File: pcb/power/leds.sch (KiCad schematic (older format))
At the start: 20 parts, among them P6 CONN_01X04, U3 LM324QT

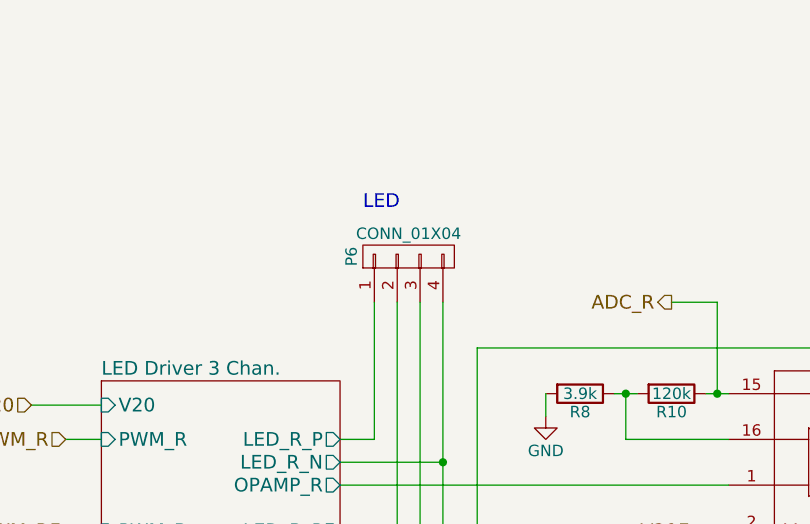
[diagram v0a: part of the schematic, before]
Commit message: Started layouting. Interfacing problems have to be discussed.
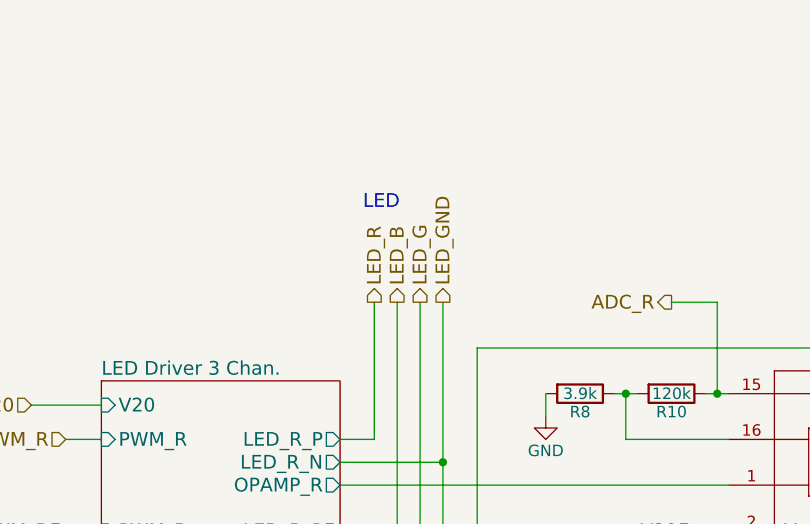
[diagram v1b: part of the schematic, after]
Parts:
- removed P6: CONN_01X04, Connect:PINHEAD1-3, symbol CONN_01X04
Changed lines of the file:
@@
-$EndComp
-$Comp
-L CONN_01X04 P6
-U 1 1 58430FB4
-P 4000 2500
-F 0 "P6" H 4000 2750 50  0000 C CNN
-F 1 "CONN_01X04" V 4100 2500 50  0000 C CNN
-F 2 "Connect:PINHEAD1-3" H 4000 2500 50  0001 C CNN
-F 3 "http://www.on-shore.com/wp-content/uploads/2015/09/ostvnxxa150.pdf" H 4000 2500 50  0001 C CNN
-F 4 "ED10563-ND" H 4000 2500 60  0001 C CNN "Digikey"
-	1    4000 2500
-	0    -1   -1   0
 $EndComp
 $Comp
@@
 Text HLabel 7450 2150 2    60   Output ~ 0
 VOLED
+Text HLabel 3850 2700 1    60   Output ~ 0
+LED_R
+Text HLabel 3950 2700 1    60   Output ~ 0
+LED_B
+Text HLabel 4050 2700 1    60   Output ~ 0
+LED_G
+Text HLabel 4150 2700 1    60   Output ~ 0
+LED_GND
 $EndSCHEMATC

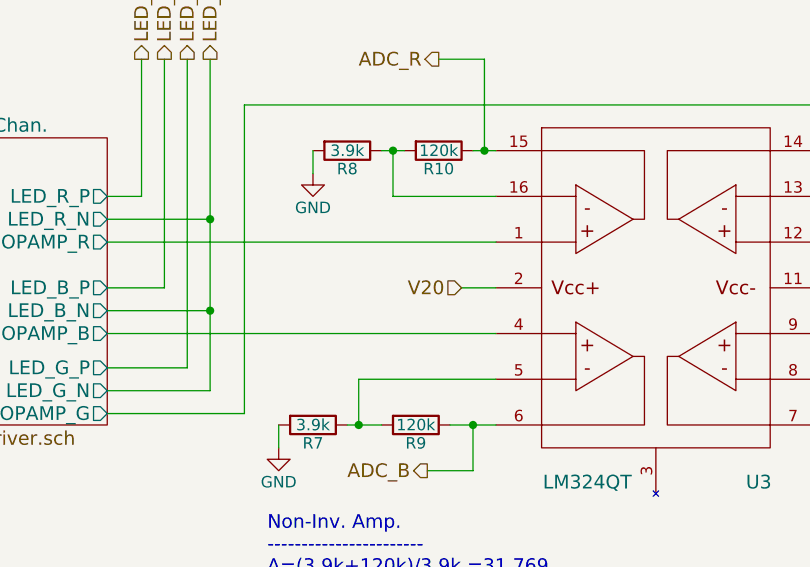
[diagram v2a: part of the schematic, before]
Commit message: Did a lot of stuff. Currently working on the exact 3D models for the headers.
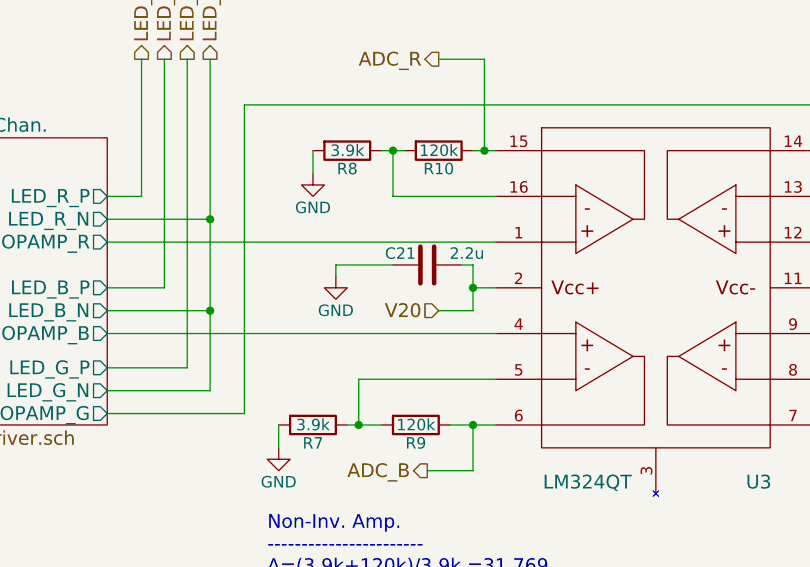
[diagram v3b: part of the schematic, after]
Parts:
- added C21: 2.2u, Capacitors_SMD:C_0603_HandSoldering, symbol C
- R10, R11, R12, R13, R14, R15, R16, R17, R18, R19, R20, R7, R8, R9: footprint Resistors_SMD:R_0603_HandSoldering -> Additional:R_0603_HandSoldering_Same_As_C
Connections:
- net GND: now also C21.1
- net V20: now also C21.2
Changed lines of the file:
@@
 $EndComp
 $Comp
-L GND #PWR015
+L GND #PWR016
 U 1 1 58430F99
 P 4600 3200
-F 0 "#PWR015" H 4600 2950 50  0001 C CNN
+F 0 "#PWR016" H 4600 2950 50  0001 C CNN
 F 1 "GND" H 4600 3050 50  0000 C CNN
 F 2 "" H 4600 3200 50  0000 C CNN
@@
 F 0 "R9" V 5130 4300 50  0000 C CNN
 F 1 "120k" V 5050 4300 50  0000 C CNN
-F 2 "Resistors_SMD:R_0603_HandSoldering" V 4980 4300 50  0001 C CNN
+F 2 "Additional:R_0603_HandSoldering_Same_As_C" V 4980 4300 50  0001 C CNN
 F 3 "http://www.yageo.com.tw/exep/pages/download/literatures/PYu-R_INT-thick_7.pdf" H 5050 4300 50  0001 C CNN
 F 4 "311-120KHRCT-ND" V 5050 4300 60  0001 C CNN "Digikey"
@@
 $EndComp
 $Comp
-L GND #PWR016
+L GND #PWR017
 U 1 1 58430FA7
 P 4450 4400
-F 0 "#PWR016" H 4450 4150 50  0001 C CNN
+F 0 "#PWR017" H 4450 4150 50  0001 C CNN
 F 1 "GND" H 4450 4250 50  0000 C CNN
 F 2 "" H 4450 4400 50  0000 C CNN
@@
 $EndComp
 $Comp
-L GND #PWR017
+L GND #PWR018
 U 1 1 58430FAD
 P 7700 4350
-F 0 "#PWR017" H 7700 4100 50  0001 C CNN
+F 0 "#PWR018" H 7700 4100 50  0001 C CNN
 F 1 "GND" H 7700 4200 50  0000 C CNN
 F 2 "" H 7700 4350 50  0000 C CNN
@@
 F 0 "R12" V 7180 3100 50  0000 C CNN
 F 1 "240k" V 7100 3100 50  0000 C CNN
-F 2 "Resistors_SMD:R_0603_HandSoldering" V 7030 3100 50  0001 C CNN
+F 2 "Additional:R_0603_HandSoldering_Same_As_C" V 7030 3100 50  0001 C CNN
 F 3 "http://www.yageo.com.tw/exep/pages/download/literatures/PYu-R_INT-thick_7.pdf" H 7100 3100 50  0001 C CNN
 F 4 "311-240KHRCT-ND" V 7100 3100 60  0001 C CNN "Digikey"
@@
 F 0 "R16" V 7680 3100 50  0000 C CNN
 F 1 "39k" V 7600 3100 50  0000 C CNN
-F 2 "Resistors_SMD:R_0603_HandSoldering" V 7530 3100 50  0001 C CNN
+F 2 "Additional:R_0603_HandSoldering_Same_As_C" V 7530 3100 50  0001 C CNN
 F 3 "http://www.yageo.com.tw/exep/pages/download/literatures/PYu-R_INT-thick_7.pdf" H 7600 3100 50  0001 C CNN
 F 4 "311-39.0KHRCT-ND" V 7600 3100 60  0001 C CNN "Digikey"
@@
 $EndComp
 $Comp
-L GND #PWR018
+L GND #PWR019
 U 1 1 58430FCB
 P 7750 3400
-F 0 "#PWR018" H 7750 3150 50  0001 C CNN
+F 0 "#PWR019" H 7750 3150 50  0001 C CNN
 F 1 "GND" H 7750 3250 50  0000 C CNN
 F 2 "" H 7750 3400 50  0000 C CNN
@@
 F 0 "R18" V 8180 3650 50  0000 C CNN
 F 1 "47k" V 8100 3650 50  0000 C CNN
-F 2 "Resistors_SMD:R_0603_HandSoldering" V 8030 3650 50  0001 C CNN
+F 2 "Additional:R_0603_HandSoldering_Same_As_C" V 8030 3650 50  0001 C CNN
 F 3 "http://www.yageo.com.tw/exep/pages/download/literatures/PYu-R_INT-thick_7.pdf" H 8100 3650 50  0001 C CNN
 F 4 "311-47.0KHRCT-ND" V 8100 3650 60  0001 C CNN "Digikey"
@@
 $EndComp
 $Comp
-L GND #PWR019
+L GND #PWR020
 U 1 1 58430FE1
 P 9100 4150
-F 0 "#PWR019" H 9100 3900 50  0001 C CNN
+F 0 "#PWR020" H 9100 3900 50  0001 C CNN
 F 1 "GND" H 9100 4000 50  0000 C CNN
 F 2 "" H 9100 4150 50  0000 C CNN
@@
 F 0 "R8" V 4830 3100 50  0000 C CNN
 F 1 "3.9k" V 4750 3100 50  0000 C CNN
-F 2 "Resistors_SMD:R_0603_HandSoldering" V 4680 3100 50  0001 C CNN
+F 2 "Additional:R_0603_HandSoldering_Same_As_C" V 4680 3100 50  0001 C CNN
 F 3 "http://www.yageo.com.tw/exep/pages/download/literatures/PYu-R_INT-thick_7.pdf" H 4750 3100 50  0001 C CNN
 F 4 "311-3.90KHRCT-ND" V 4750 3100 60  0001 C CNN "Digikey"
@@
 F 0 "R10" V 5230 3100 50  0000 C CNN
 F 1 "120k" V 5150 3100 50  0000 C CNN
-F 2 "Resistors_SMD:R_0603_HandSoldering" V 5080 3100 50  0001 C CNN
+F 2 "Additional:R_0603_HandSoldering_Same_As_C" V 5080 3100 50  0001 C CNN
 F 3 "http://www.yageo.com.tw/exep/pages/download/literatures/PYu-R_INT-thick_7.pdf" H 5150 3100 50  0001 C CNN
 F 4 "311-120KHRCT-ND" V 5150 3100 60  0001 C CNN "Digikey"
@@
 F 0 "R13" V 7180 4300 50  0000 C CNN
 F 1 "120k" V 7100 4300 50  0000 C CNN
-F 2 "Resistors_SMD:R_0603_HandSoldering" V 7030 4300 50  0001 C CNN
+F 2 "Additional:R_0603_HandSoldering_Same_As_C" V 7030 4300 50  0001 C CNN
 F 3 "http://www.yageo.com.tw/exep/pages/download/literatures/PYu-R_INT-thick_7.pdf" H 7100 4300 50  0001 C CNN
 F 4 "311-120KHRCT-ND" V 7100 4300 60  0001 C CNN "Digikey"
@@
 F 0 "R7" V 4680 4300 50  0000 C CNN
 F 1 "3.9k" V 4600 4300 50  0000 C CNN
-F 2 "Resistors_SMD:R_0603_HandSoldering" V 4530 4300 50  0001 C CNN
+F 2 "Additional:R_0603_HandSoldering_Same_As_C" V 4530 4300 50  0001 C CNN
 F 3 "http://www.yageo.com.tw/exep/pages/download/literatures/PYu-R_INT-thick_7.pdf" H 4600 4300 50  0001 C CNN
 F 4 "311-3.90KHRCT-ND" V 4600 4300 60  0001 C CNN "Digikey"
@@
 F 0 "R14" V 7630 4300 50  0000 C CNN
 F 1 "3.9k" V 7550 4300 50  0000 C CNN
-F 2 "Resistors_SMD:R_0603_HandSoldering" V 7480 4300 50  0001 C CNN
+F 2 "Additional:R_0603_HandSoldering_Same_As_C" V 7480 4300 50  0001 C CNN
 F 3 "http://www.yageo.com.tw/exep/pages/download/literatures/PYu-R_INT-thick_7.pdf" H 7550 4300 50  0001 C CNN
 F 4 "311-3.90KHRCT-ND" V 7550 4300 60  0001 C CNN "Digikey"
@@
 F 0 "R19" V 8580 3650 50  0000 C CNN
 F 1 "47k" V 8500 3650 50  0000 C CNN
-F 2 "Resistors_SMD:R_0603_HandSoldering" V 8430 3650 50  0001 C CNN
+F 2 "Additional:R_0603_HandSoldering_Same_As_C" V 8430 3650 50  0001 C CNN
 F 3 "http://www.yageo.com.tw/exep/pages/download/literatures/PYu-R_INT-thick_7.pdf" H 8500 3650 50  0001 C CNN
 F 4 "311-47.0KHRCT-ND" V 8500 3650 60  0001 C CNN "Digikey"
@@
 F 0 "R20" V 8980 3650 50  0000 C CNN
 F 1 "47k" V 8900 3650 50  0000 C CNN
-F 2 "Resistors_SMD:R_0603_HandSoldering" V 8830 3650 50  0001 C CNN
+F 2 "Additional:R_0603_HandSoldering_Same_As_C" V 8830 3650 50  0001 C CNN
 F 3 "http://www.yageo.com.tw/exep/pages/download/literatures/PYu-R_INT-thick_7.pdf" H 8900 3650 50  0001 C CNN
 F 4 "311-47.0KHRCT-ND" V 8900 3650 60  0001 C CNN "Digikey"
@@
 $EndComp
 $Comp
-L GND #PWR020
+L GND #PWR021
 U 1 1 58431031
 P 7000 3700
-F 0 "#PWR020" H 7000 3450 50  0001 C CNN
+F 0 "#PWR021" H 7000 3450 50  0001 C CNN
 F 1 "GND" H 7000 3550 50  0000 C CNN
 F 2 "" H 7000 3700 50  0000 C CNN
@@
 F 0 "R11" V 7180 2500 50  0000 C CNN
 F 1 "120k" V 7100 2500 50  0000 C CNN
-F 2 "Resistors_SMD:R_0603_HandSoldering" V 7030 2500 50  0001 C CNN
+F 2 "Additional:R_0603_HandSoldering_Same_As_C" V 7030 2500 50  0001 C CNN
 F 3 "http://www.yageo.com.tw/exep/pages/download/literatures/PYu-R_INT-thick_7.pdf" H 7100 2500 50  0001 C CNN
 F 4 "311-120KHRCT-ND" V 7100 2500 60  0001 C CNN "Digikey"
@@
 F 0 "R15" V 7680 2500 50  0000 C CNN
 F 1 "2.7k" V 7600 2500 50  0000 C CNN
-F 2 "Resistors_SMD:R_0603_HandSoldering" V 7530 2500 50  0001 C CNN
+F 2 "Additional:R_0603_HandSoldering_Same_As_C" V 7530 2500 50  0001 C CNN
 F 3 "http://www.yageo.com.tw/exep/pages/download/literatures/PYu-R_INT-thick_7.pdf" H 7600 2500 50  0001 C CNN
 F 4 "311-2.70KHRCT-ND" V 7600 2500 60  0001 C CNN "Digikey"
@@
 F 0 "R17" V 8030 2500 50  0000 C CNN
 F 1 "3.3k" V 7950 2500 50  0000 C CNN
-F 2 "Resistors_SMD:R_0603_HandSoldering" V 7880 2500 50  0001 C CNN
+F 2 "Additional:R_0603_HandSoldering_Same_As_C" V 7880 2500 50  0001 C CNN
 F 3 "http://www.yageo.com.tw/exep/pages/download/literatures/PYu-R_INT-thick_7.pdf" H 7950 2500 50  0001 C CNN
 F 4 "311-3.30KHRCT-ND" V 7950 2500 60  0001 C CNN "Digikey"
@@
 $EndComp
 $Comp
-L GND #PWR021
+L GND #PWR022
 U 1 1 58431051
 P 8100 2900
-F 0 "#PWR021" H 8100 2650 50  0001 C CNN
+F 0 "#PWR022" H 8100 2650 50  0001 C CNN
 F 1 "GND" H 8100 2750 50  0000 C CNN
 F 2 "" H 8100 2900 50  0000 C CNN
@@
 Wire Wire Line
 	4150 2700 4150 4150
-Wire Wire Line
-	5250 3700 5400 3700
 Wire Wire Line
 	7850 3900 6800 3900
@@
 Text HLabel 5150 2700 0    60   Output ~ 0
 ADC_R
-Text HLabel 5250 3700 0    60   Input ~ 0
+Text HLabel 5150 3800 0    60   Input ~ 0
 V20
 Text HLabel 5100 4500 0    60   Output ~ 0
@@
 Text HLabel 4150 2700 1    60   Output ~ 0
 LED_GND
+$Comp
+L C C21
+U 1 1 584CBAE2
+P 5100 3600
+F 0 "C21" V 5150 3650 50  0000 L CNN
+F 1 "2.2u" V 5150 3350 50  0000 L CNN
+F 2 "Capacitors_SMD:C_0603_HandSoldering" H 5138 3450 50  0001 C CNN
+F 3 "http://search.murata.co.jp/Ceramy/image/img/A01X/partnumbering_e_01.pdf" H 5100 3600 50  0001 C CNN
+F 4 "490-7204-1-ND" H 5100 3600 60  0001 C CNN "Digikey"
+	1    5100 3600
+	0    -1   -1   0
+$EndComp
+$Comp
+L GND #PWR023
+U 1 1 584CCA77
+P 4700 3650
+F 0 "#PWR023" H 4700 3400 50  0001 C CNN
+F 1 "GND" H 4700 3500 50  0000 C CNN
+F 2 "" H 4700 3650 50  0000 C CNN
+F 3 "" H 4700 3650 50  0000 C CNN
+	1    4700 3650
+	1    0    0    -1
+$EndComp
+Wire Wire Line
+	5400 3700 5300 3700
+Wire Wire Line
+	5300 3600 5300 3800
+Wire Wire Line
+	5300 3600 5250 3600
+Connection ~ 5300 3700
+Wire Wire Line
+	4700 3650 4700 3600
+Wire Wire Line
+	4700 3600 4950 3600
+Wire Wire Line
+	5300 3800 5150 3800
 $EndSCHEMATC

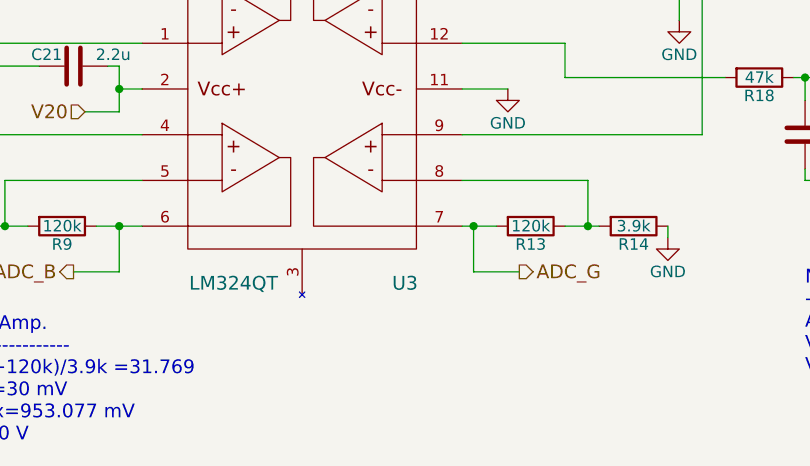
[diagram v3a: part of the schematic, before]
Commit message: Started completely over with the layout, as the OLED would not fit anymore. Also introduced a USB DCP Controller and found a stupid bug in the LED driver.
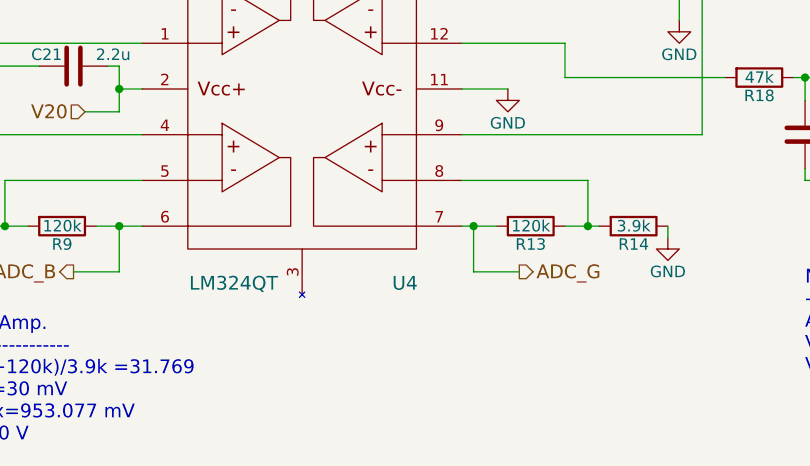
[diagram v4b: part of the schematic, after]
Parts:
- renumbered U3 to U4
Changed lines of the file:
@@
 $EndSheet
 $Comp
-L LM324QT U3
+L LM324QT U4
 U 1 1 58430F92
 P 6100 3700
-F 0 "U3" H 6550 2850 60  0000 C CNN
+F 0 "U4" H 6550 2850 60  0000 C CNN
 F 1 "LM324QT" H 5800 2850 60  0000 C CNN
 F 2 "Additional:QFN-16-1EP_3x3mm_Pitch0.5mm" H 6100 3700 60  0001 C CNN
@@
 $EndComp
 $Comp
-L GND #PWR016
+L GND #PWR16
 U 1 1 58430F99
 P 4600 3200
-F 0 "#PWR016" H 4600 2950 50  0001 C CNN
+F 0 "#PWR16" H 4600 2950 50  0001 C CNN
 F 1 "GND" H 4600 3050 50  0000 C CNN
 F 2 "" H 4600 3200 50  0000 C CNN
@@
 $EndComp
 $Comp
-L GND #PWR017
+L GND #PWR15
 U 1 1 58430FA7
 P 4450 4400
-F 0 "#PWR017" H 4450 4150 50  0001 C CNN
+F 0 "#PWR15" H 4450 4150 50  0001 C CNN
 F 1 "GND" H 4450 4250 50  0000 C CNN
 F 2 "" H 4450 4400 50  0000 C CNN
@@
 $EndComp
 $Comp
-L GND #PWR018
+L GND #PWR19
 U 1 1 58430FAD
 P 7700 4350
-F 0 "#PWR018" H 7700 4100 50  0001 C CNN
+F 0 "#PWR19" H 7700 4100 50  0001 C CNN
 F 1 "GND" H 7700 4200 50  0000 C CNN
 F 2 "" H 7700 4350 50  0000 C CNN
@@
 $EndComp
 $Comp
-L GND #PWR019
+L GND #PWR20
 U 1 1 58430FCB
 P 7750 3400
-F 0 "#PWR019" H 7750 3150 50  0001 C CNN
+F 0 "#PWR20" H 7750 3150 50  0001 C CNN
 F 1 "GND" H 7750 3250 50  0000 C CNN
 F 2 "" H 7750 3400 50  0000 C CNN
@@
 $EndComp
 $Comp
-L GND #PWR020
+L GND #PWR22
 U 1 1 58430FE1
 P 9100 4150
-F 0 "#PWR020" H 9100 3900 50  0001 C CNN
+F 0 "#PWR22" H 9100 3900 50  0001 C CNN
 F 1 "GND" H 9100 4000 50  0000 C CNN
 F 2 "" H 9100 4150 50  0000 C CNN
@@
 $EndComp
 $Comp
-L GND #PWR021
+L GND #PWR18
 U 1 1 58431031
 P 7000 3700
-F 0 "#PWR021" H 7000 3450 50  0001 C CNN
+F 0 "#PWR18" H 7000 3450 50  0001 C CNN
 F 1 "GND" H 7000 3550 50  0000 C CNN
 F 2 "" H 7000 3700 50  0000 C CNN
@@
 $EndComp
 $Comp
-L GND #PWR022
+L GND #PWR21
 U 1 1 58431051
 P 8100 2900
-F 0 "#PWR022" H 8100 2650 50  0001 C CNN
+F 0 "#PWR21" H 8100 2650 50  0001 C CNN
 F 1 "GND" H 8100 2750 50  0000 C CNN
 F 2 "" H 8100 2900 50  0000 C CNN
@@
 $EndComp
 $Comp
-L GND #PWR023
+L GND #PWR17
 U 1 1 584CCA77
 P 4700 3650
-F 0 "#PWR023" H 4700 3400 50  0001 C CNN
+F 0 "#PWR17" H 4700 3400 50  0001 C CNN
 F 1 "GND" H 4700 3500 50  0000 C CNN
 F 2 "" H 4700 3650 50  0000 C CNN

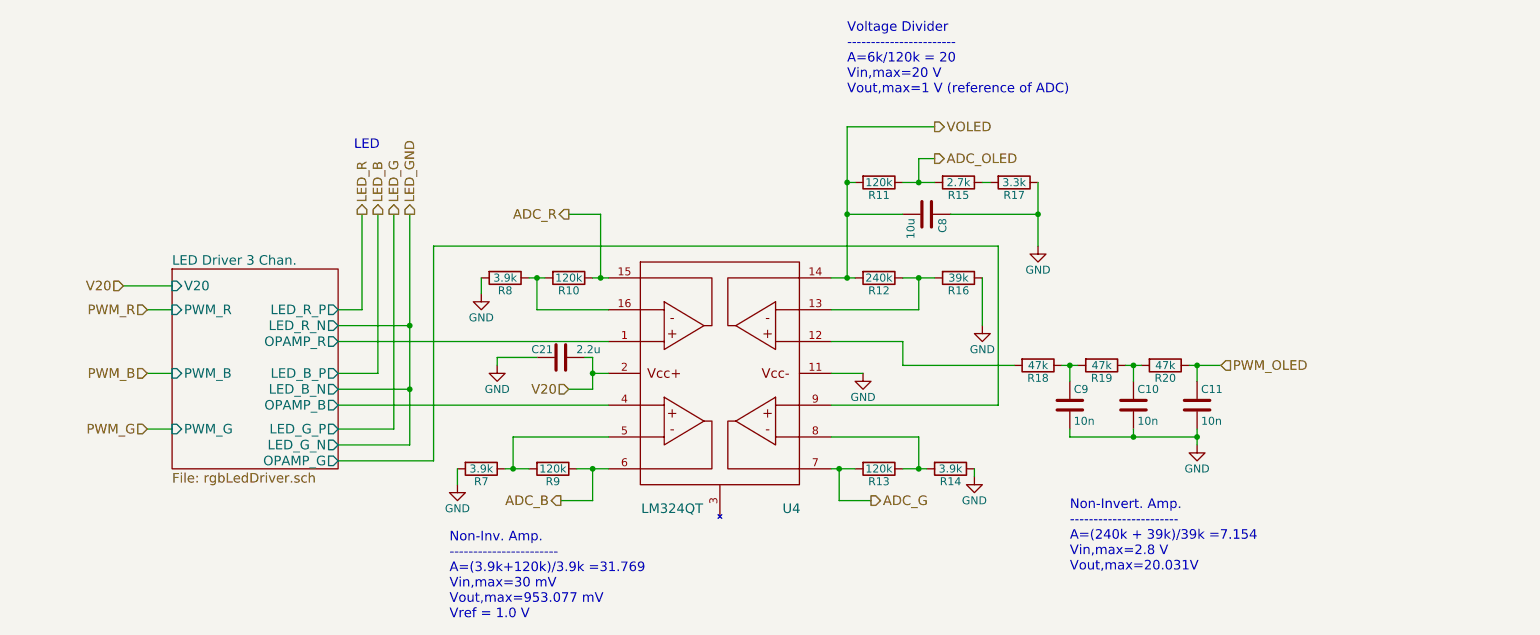
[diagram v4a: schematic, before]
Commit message: Fixed the bug. Now workin with differential amplifiers. Started over once more with the layout.
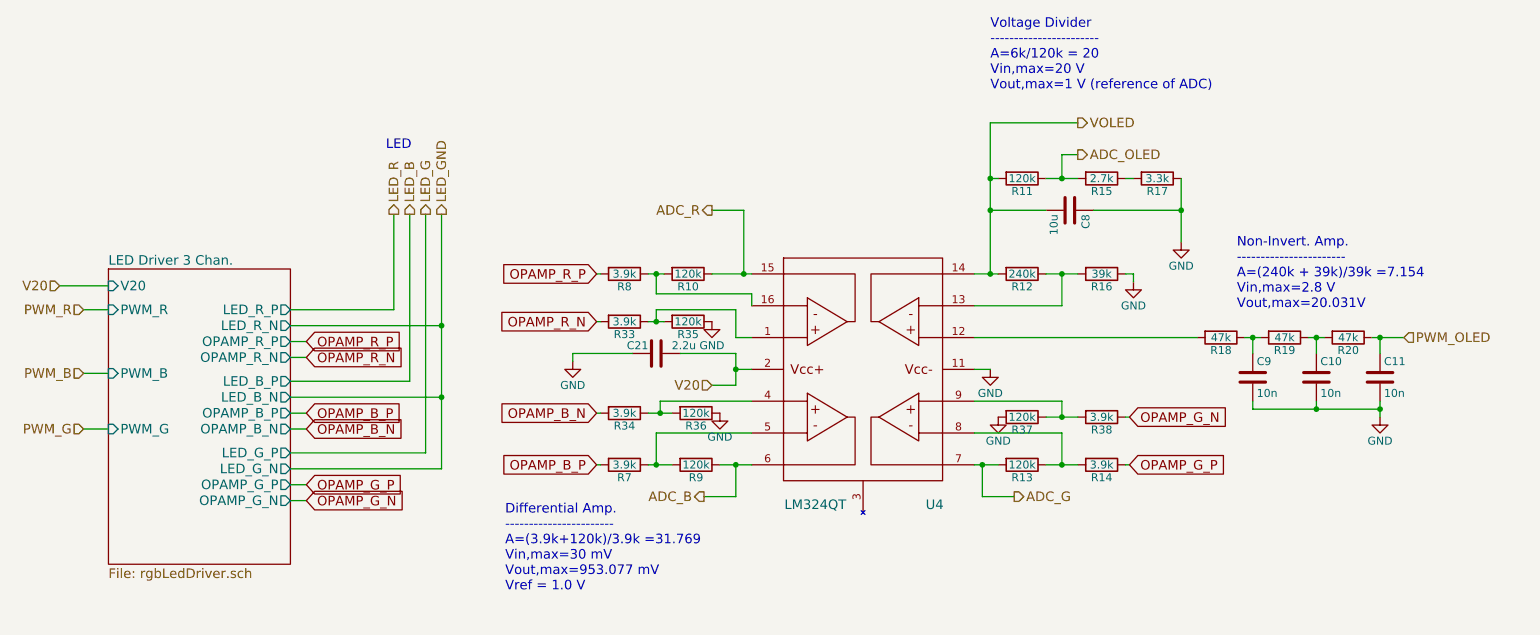
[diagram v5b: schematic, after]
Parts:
- added R33, R34, R38: 3.9k, Additional:R_0603_HandSoldering_Same_As_C, symbol R
- added R35, R36, R37: 120k, Additional:R_0603_HandSoldering_Same_As_C, symbol R
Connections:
- net GND: now also R35.1, R36.1, R37.2; no longer R14.1, R7.2, R8.2
- net LED Driver 3 Chan. /OPAMP_B: no longer names the net of U4.4 (P_2)
- net LED Driver 3 Chan. /OPAMP_B: now also R34.1, R36.2
- net LED Driver 3 Chan. /OPAMP_G: no longer names the net of U4.9 (P_3)
- net LED Driver 3 Chan. /OPAMP_G: now also R37.1, R38.2
- net LED Driver 3 Chan. /OPAMP_R: no longer names the net of U4.1 (P_1)
- net LED Driver 3 Chan. /OPAMP_R: now also R33.1, R35.2
- new net OPAMP_B_N: R34.2
- new net OPAMP_B_P: R7.2
- new net OPAMP_G_N: R38.1
- new net OPAMP_G_P: R14.1
- new net OPAMP_R_N: R33.2
- new net OPAMP_R_P: R8.2
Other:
- note added: "Differential Amp.\n-----------------------\nA=(3.9k+120k)/3.9k =31.769\nVin,max=30 mV\nVout,max=953.077 mV\nVref = 1.0 V"
- note removed: "Non-Inv. Amp.\n-----------------------\nA=(3.9k+120k)/3.9k =31.769\nVin,max=30 mV\nVout,max=953.077 mV\nVref = 1.0 V"
- moved on the sheet: C10, C11, C21, C8, C9, R10, R11, R12, R13, R14, R15, R16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
